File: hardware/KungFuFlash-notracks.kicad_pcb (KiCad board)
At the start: 2 copper layers, 62 x 83.6 mm, 46 parts, among them J1 USB Power, J2 USB_B_Mini, J4 SWD, Q1 BC817, SW1 Reset, SW2 Menu, SW3 Special, U1 C64-Exp-Port, U2 AMS1117-3.3, U3 STM32F405RGTx, Y1 8MHz

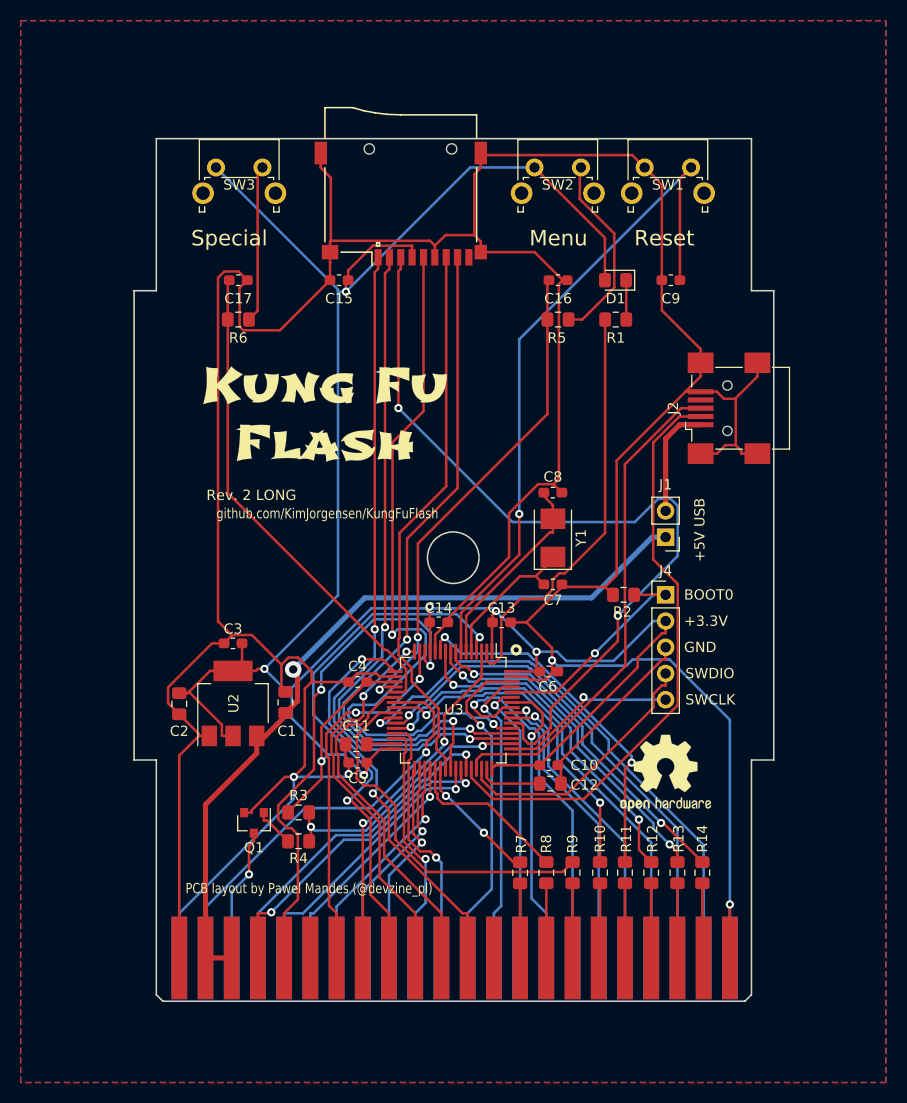
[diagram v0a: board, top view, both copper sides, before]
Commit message: Trace routing and layout cleanup.
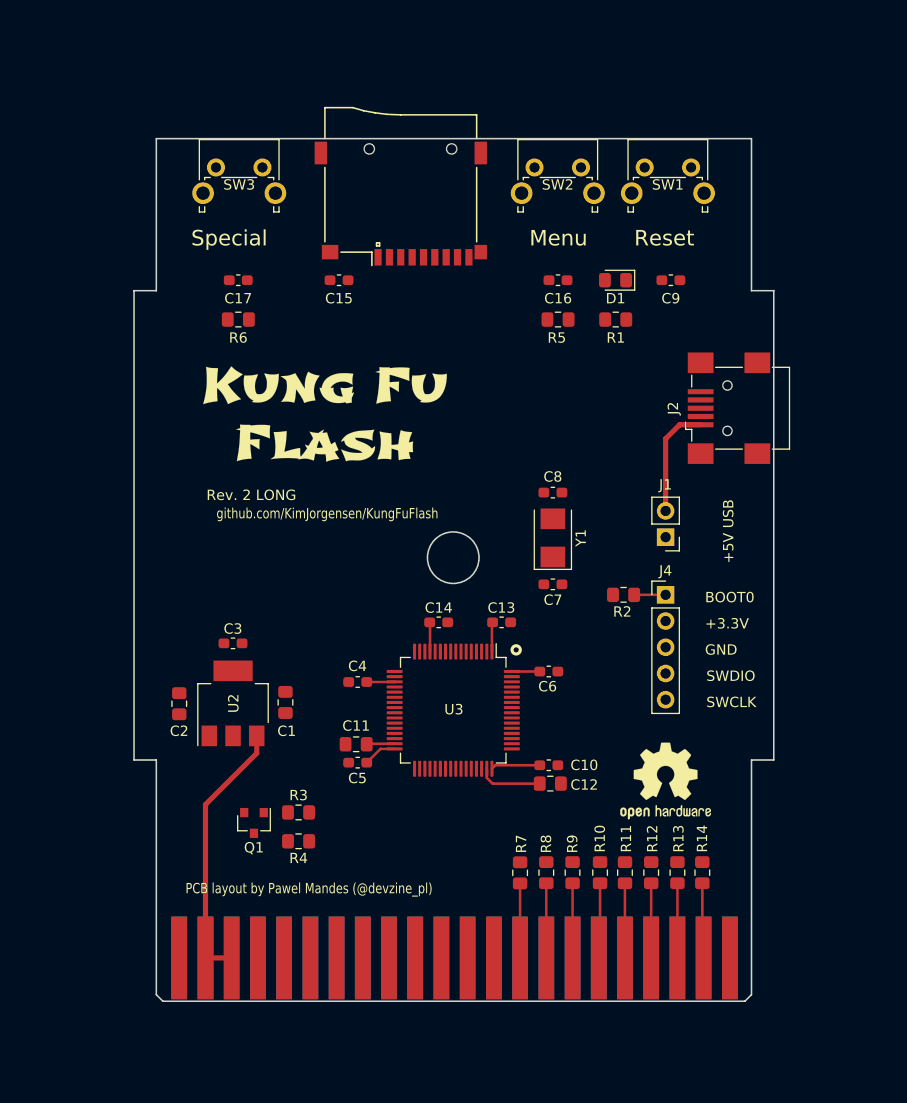
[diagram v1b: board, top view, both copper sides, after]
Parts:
- moved REF** 0.76 mm to (121.0, 118.5)
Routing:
- net GND: track 425.5 -> 0.00 mm, vias 4 -> 0
- net +3V3: track 243.5 -> 19.2 mm, vias 7 -> 0
- net /SD_CMD: track 80.1 -> 0.00 mm, vias 2 -> 0
- net /SD_CK: track 71.9 -> 0.00 mm, vias 2 -> 0
- net /~RST: track 67.5 -> 0.00 mm, vias 1 -> 0
- net /SD_D1: track 66.2 -> 0.00 mm, vias 2 -> 0
- net /SD_D2: track 65.9 -> 0.00 mm, vias 2 -> 0
- net /SD_D3: track 65.4 -> 0.00 mm, vias 2 -> 0
- net /USB_DM: track 57.5 -> 0.00 mm
- net /A0: track 54.3 -> 0.00 mm, vias 1 -> 0
- net /~EXROM: track 54.0 -> 0.00 mm, vias 2 -> 0
- net /SD_D0: track 53.5 -> 0.00 mm
- net +5V: track 76.6 -> 26.1 mm, vias 1 -> 0
- net /A1: track 49.6 -> 0.00 mm, vias 1 -> 0
- net /R~W: track 49.1 -> 0.00 mm, vias 2 -> 0
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- removed copper zone on B.Cu, net GND
- removed copper zone on F.Cu, net GND
